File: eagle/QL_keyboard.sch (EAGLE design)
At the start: 40 parts, among them J1 USB-A-S, J2 AVR_SPI_PRG_6TESTPOINTS, U2 3.3V/150mA, U3 MAX3421ESMD, U4 ATMEGA328P_TQFP, U5 TXB0108PW-TSSOP20, Y1 8MHZ

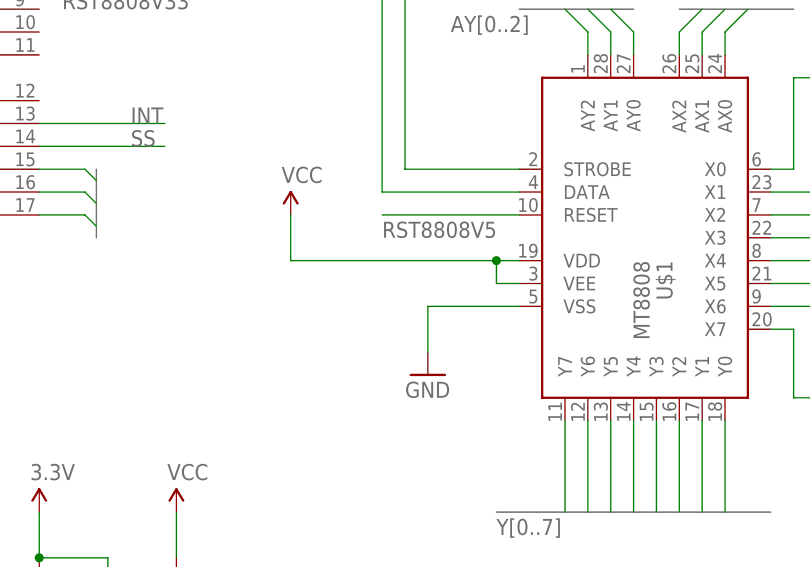
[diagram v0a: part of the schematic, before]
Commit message: Fix bug in MT8808 VEE connection: connect to GND instead of VCC
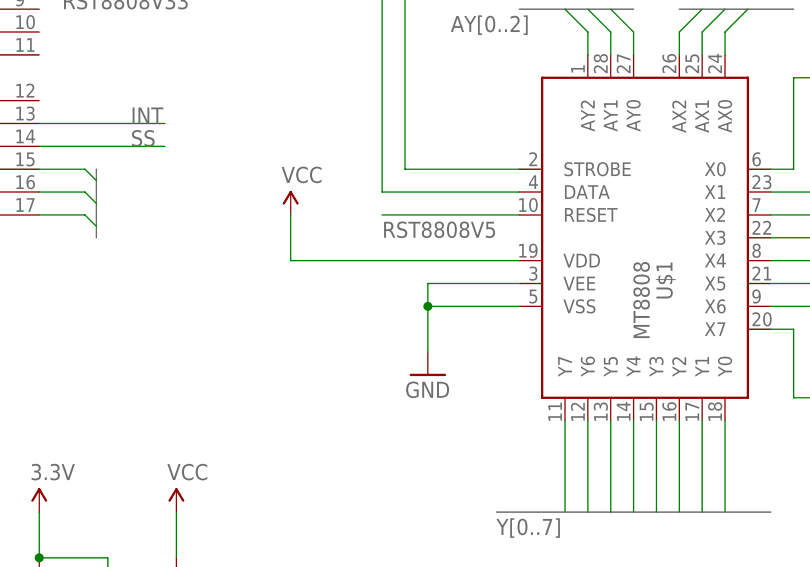
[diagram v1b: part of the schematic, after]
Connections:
- net GND: now also U$1.VEE
- net VCC: no longer U$1.VEE
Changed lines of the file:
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@@
 <pinref part="U$1" gate="G$1" pin="VDD"/>
 <pinref part="SUPPLY3" gate="G$1" pin="VCC"/>
-<wire x1="111.76" y1="35.56" x2="109.22" y2="35.56" width="0.1524" layer="91"/>
-<wire x1="109.22" y1="35.56" x2="86.36" y2="35.56" width="0.1524" layer="91"/>
+<wire x1="111.76" y1="35.56" x2="86.36" y2="35.56" width="0.1524" layer="91"/>
 <wire x1="86.36" y1="35.56" x2="86.36" y2="40.64" width="0.1524" layer="91"/>
-<pinref part="U$1" gate="G$1" pin="VEE"/>
-<wire x1="111.76" y1="33.02" x2="109.22" y2="33.02" width="0.1524" layer="91"/>
-<wire x1="109.22" y1="33.02" x2="109.22" y2="35.56" width="0.1524" layer="91"/>
-<junction x="109.22" y="35.56"/>
 </segment>
 <segment>
@@
 <wire x1="111.76" y1="30.48" x2="101.6" y2="30.48" width="0.1524" layer="91"/>
 <wire x1="101.6" y1="30.48" x2="101.6" y2="25.4" width="0.1524" layer="91"/>
+<pinref part="U$1" gate="G$1" pin="VEE"/>
+<wire x1="111.76" y1="33.02" x2="101.6" y2="33.02" width="0.1524" layer="91"/>
+<wire x1="101.6" y1="33.02" x2="101.6" y2="30.48" width="0.1524" layer="91"/>
+<junction x="101.6" y="30.48"/>
 </segment>
 <segment>

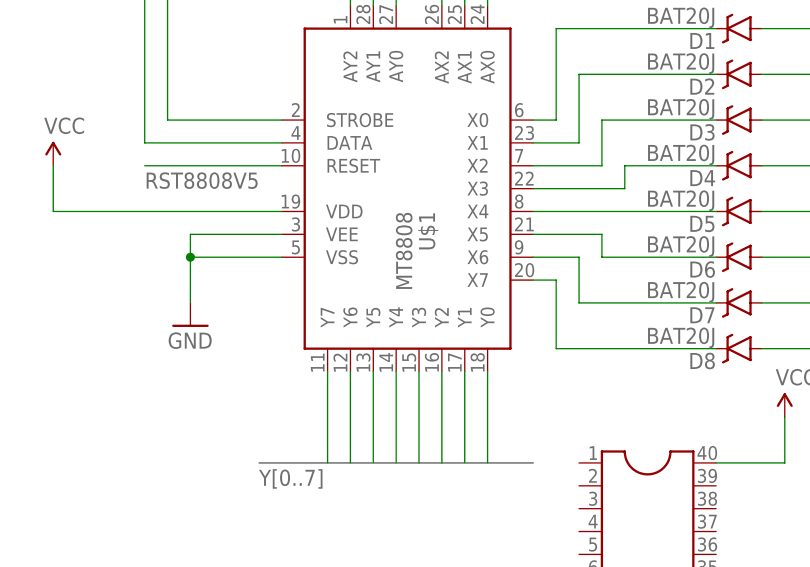
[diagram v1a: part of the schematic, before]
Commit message: Change MT8808 package to SMD PLCC28 holder.
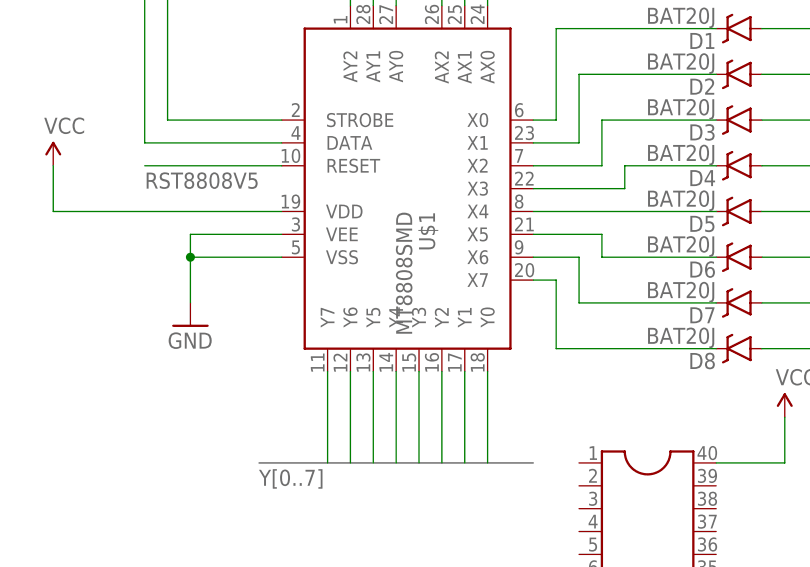
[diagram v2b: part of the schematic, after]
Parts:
- U$1: value MT8808 -> MT8808SMD; device ppe_custom:MT8808 -> ppe_custom:MT8808SMD

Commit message: Replace FTDI header with a two pin RXI/TXO header.
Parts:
- removed C10: 0.1uF, SparkFun-Capacitors:2.2UF-10V-20%(0603)
- removed FTDI: 1, SparkFun-Connectors:ARDUINO_SERIAL_PROGRAMPTH
- added COMMS: (no value), ppe_custom:M02PTH
- Y1: device SparkFun-FreqCtrl:RESONATOR8MHZ -> ppe_custom:RESONATOR8MHZ
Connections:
- removed net DTR: C10.1, FTDI.DTR
- net 3.3V: no longer FTDI.VCC
- net GND: no longer FTDI.CTS, FTDI.GND
- net RST: no longer C10.2
- net RXI: now also COMMS.1; no longer FTDI.RXI
- net TXO: now also COMMS.2; no longer FTDI.TXO

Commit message: Move ISP header and fix USB connector footprint
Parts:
- J1: device SparkFun-Connectors:USB-A-S -> ppe_custom:USB-A-S
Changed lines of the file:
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@@
 <part name="U3" library="SparkFun-DigitalIC" deviceset="MAX3421E" device="SMD"/>
 <part name="U4" library="SparkFun-DigitalIC" deviceset="ATMEGA328P_TQFP" device="" value="ATMEGA328P_TQFP"/>
-<part name="J1" library="SparkFun-Connectors" deviceset="USB" device="-A-S"/>
 <part name="R3" library="SparkFun-Resistors" deviceset="33OHM1/10W1%(0603)" device="" value="33"/>
 <part name="R4" library="SparkFun-Resistors" deviceset="33OHM1/10W1%(0603)" device="" value="33"/>
@@
 <part name="Y1" library="ppe_custom" deviceset="RESONATOR" device="8MHZ" value="8MHZ"/>
 <part name="COMMS" library="ppe_custom" deviceset="M02" device="PTH"/>
+<part name="J1" library="ppe_custom" deviceset="USB" device="-A-S"/>
 </parts>
 <sheets>
@@
 <instance part="U3" gate="G$1" x="-27.94" y="73.66" rot="R90"/>
 <instance part="U4" gate="U$1" x="35.56" y="68.58"/>
-<instance part="J1" gate="G$1" x="-68.58" y="43.18" rot="R180"/>
 <instance part="R3" gate="G$1" x="-46.99" y="38.1"/>
 <instance part="R4" gate="G$1" x="-46.99" y="30.48"/>
@@
 <instance part="Y1" gate="G$1" x="5.08" y="63.5"/>
 <instance part="COMMS" gate="G$1" x="86.36" y="-38.1"/>
+<instance part="J1" gate="G$1" x="-68.58" y="43.18" rot="R180"/>
 </instances>
 <busses>
@@
 <net name="N$1" class="0">
 <segment>
-<pinref part="J1" gate="G$1" pin="D-"/>
 <pinref part="R3" gate="G$1" pin="1"/>
 <wire x1="-66.04" y1="38.1" x2="-52.07" y2="38.1" width="0.1524" layer="91"/>
+<pinref part="J1" gate="G$1" pin="D-"/>
 </segment>
 </net>
@@
 <wire x1="-52.07" y1="30.48" x2="-55.88" y2="30.48" width="0.1524" layer="91"/>
 <wire x1="-55.88" y1="30.48" x2="-55.88" y2="35.56" width="0.1524" layer="91"/>
+<wire x1="-55.88" y1="35.56" x2="-66.04" y2="35.56" width="0.1524" layer="91"/>
 <pinref part="J1" gate="G$1" pin="D+"/>
-<wire x1="-55.88" y1="35.56" x2="-66.04" y2="35.56" width="0.1524" layer="91"/>
 </segment>
 </net>
@@
 </segment>
 <segment>
-<pinref part="J1" gate="G$1" pin="VBUS"/>
 <wire x1="-54.61" y1="40.64" x2="-66.04" y2="40.64" width="0.1524" layer="91"/>
 <label x="-59.69" y="40.64" size="1.778" layer="95"/>
+<pinref part="J1" gate="G$1" pin="VBUS"/>
 </segment>
 </net>
@@
 <wire x1="-53.34" y1="22.86" x2="-53.34" y2="43.18" width="0.1524" layer="91"/>
 <pinref part="C3" gate="G$1" pin="1"/>
-<pinref part="J1" gate="G$1" pin="GND"/>
 <wire x1="-53.34" y1="43.18" x2="-53.34" y2="46.99" width="0.1524" layer="91"/>
 <wire x1="-66.04" y1="43.18" x2="-53.34" y2="43.18" width="0.1524" layer="91"/>
 <junction x="-53.34" y="43.18"/>
-</segment>
-<segment>
+<pinref part="J1" gate="G$1" pin="GND"/>
+</segment>
+<segment>

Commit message: General cleanup of layout
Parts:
- renumbered XTAL-12MHZ to U$3
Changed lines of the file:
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@@
 <setting verticaltext="up"/>
 </settings>
-<grid distance="0.1" unitdist="inch" unit="inch" style="lines" multiple="1" display="no" altdistance="0.01" altunitdist="inch" altunit="inch"/>
+<grid distance="5" unitdist="mil" unit="mil" style="lines" multiple="1" display="no" altdistance="0.01" altunitdist="inch" altunit="inch"/>
 <layers>
 <layer number="1" name="Top" color="4" fill="1" visible="no" active="no"/>
@@
 <part name="GND3" library="SparkFun-Aesthetics" deviceset="GND" device=""/>
 <part name="SUPPLY5" library="SparkFun-Aesthetics" deviceset="3.3V" device=""/>
-<part name="XTAL-12MHZ" library="ppe_custom" deviceset="CRYSTAL-SMD" device=""/>
 <part name="GND4" library="SparkFun-Aesthetics" deviceset="GND" device=""/>
 <part name="GND5" library="SparkFun-Aesthetics" deviceset="GND" device=""/>
@@
 <part name="COMMS" library="ppe_custom" deviceset="M02" device="PTH"/>
 <part name="J1" library="ppe_custom" deviceset="USB" device="-A-S"/>
+<part name="U$3" library="ppe_custom" deviceset="CRYSTAL-SMD" device=""/>
 </parts>
 <sheets>
@@
 <instance part="GND3" gate="1" x="-71.12" y="102.87"/>
 <instance part="SUPPLY5" gate="G$1" x="-33.02" y="123.19"/>
-<instance part="XTAL-12MHZ" gate="G$1" x="-44.45" y="-11.43"/>
 <instance part="GND4" gate="1" x="-44.45" y="-26.67"/>
 <instance part="GND5" gate="1" x="-7.62" y="38.1"/>
@@
 <instance part="COMMS" gate="G$1" x="86.36" y="-38.1"/>
 <instance part="J1" gate="G$1" x="-68.58" y="43.18" rot="R180"/>
+<instance part="U$3" gate="G$1" x="-44.45" y="-11.43"/>
 </instances>
 <busses>
@@
 </segment>
 <segment>
-<pinref part="XTAL-12MHZ" gate="G$1" pin="1"/>
 <pinref part="C1" gate="G$1" pin="1"/>
 <wire x1="-46.99" y1="-11.43" x2="-54.61" y2="-11.43" width="0.1524" layer="91"/>
@@
 <junction x="-54.61" y="-11.43"/>
 <label x="-55.88" y="-6.35" size="1.778" layer="95" rot="R90"/>
+<pinref part="U$3" gate="G$1" pin="1"/>
 </segment>
 </net>
@@
 </segment>
 <segment>
-<pinref part="XTAL-12MHZ" gate="G$1" pin="2"/>
 <pinref part="C2" gate="G$1" pin="1"/>
 <wire x1="-41.91" y1="-11.43" x2="-34.29" y2="-11.43" width="0.1524" layer="91"/>
@@
 <junction x="-34.29" y="-11.43"/>
 <label x="-35.56" y="-6.35" size="1.778" layer="95" rot="R90"/>
-</segment>
-</net>
+<pinref part="U$3" gate="G$1" pin="2"/>
+</segment>
+</net>

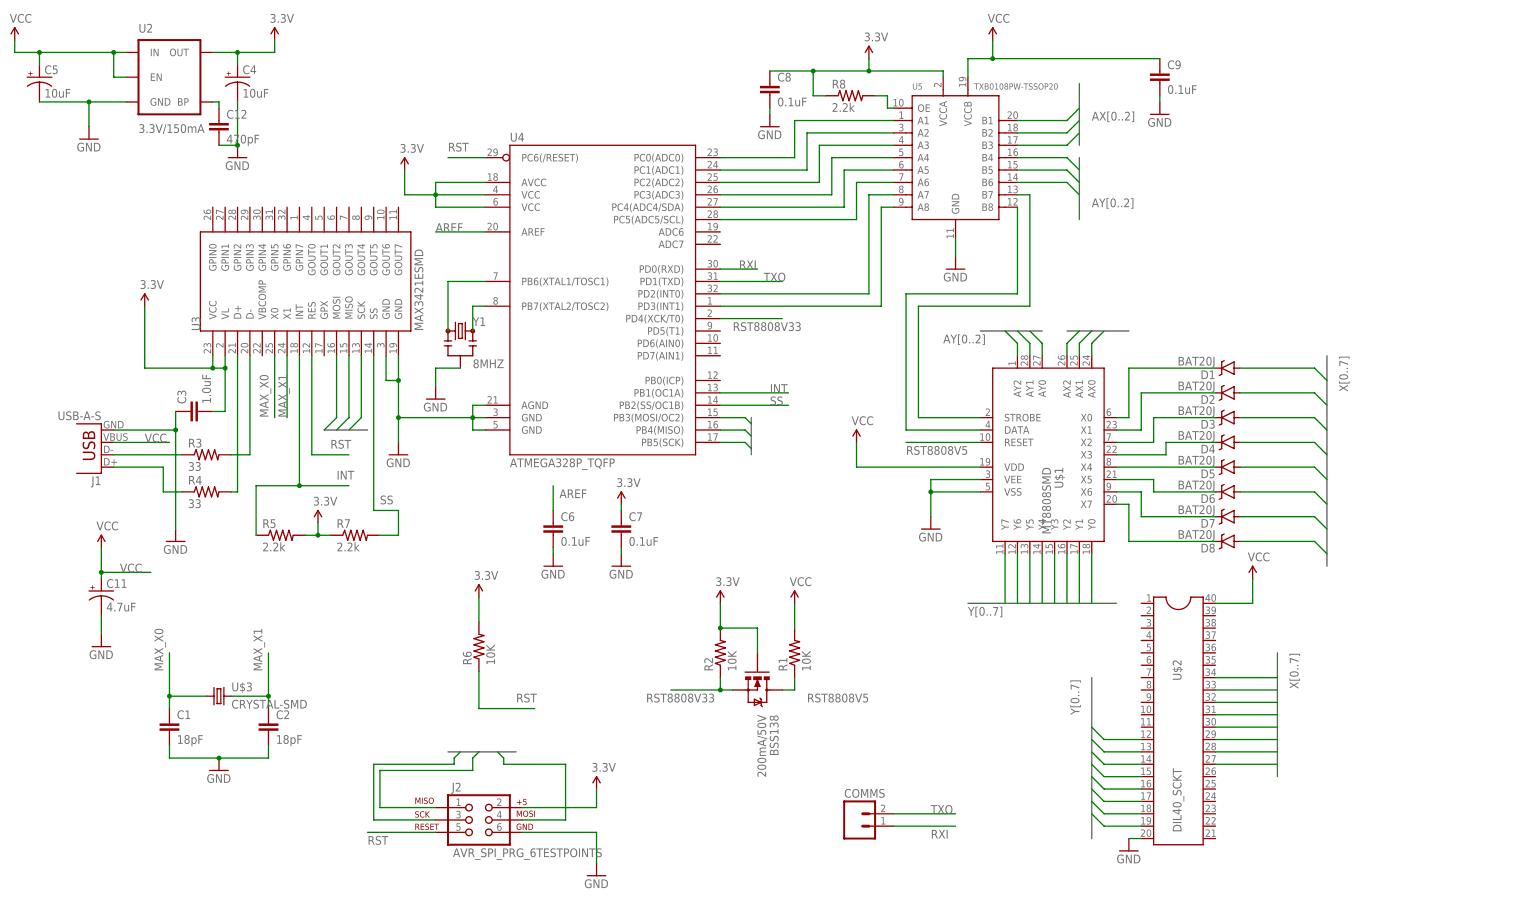
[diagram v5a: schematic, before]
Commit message: Add QL reset logic with voltage level shifting.
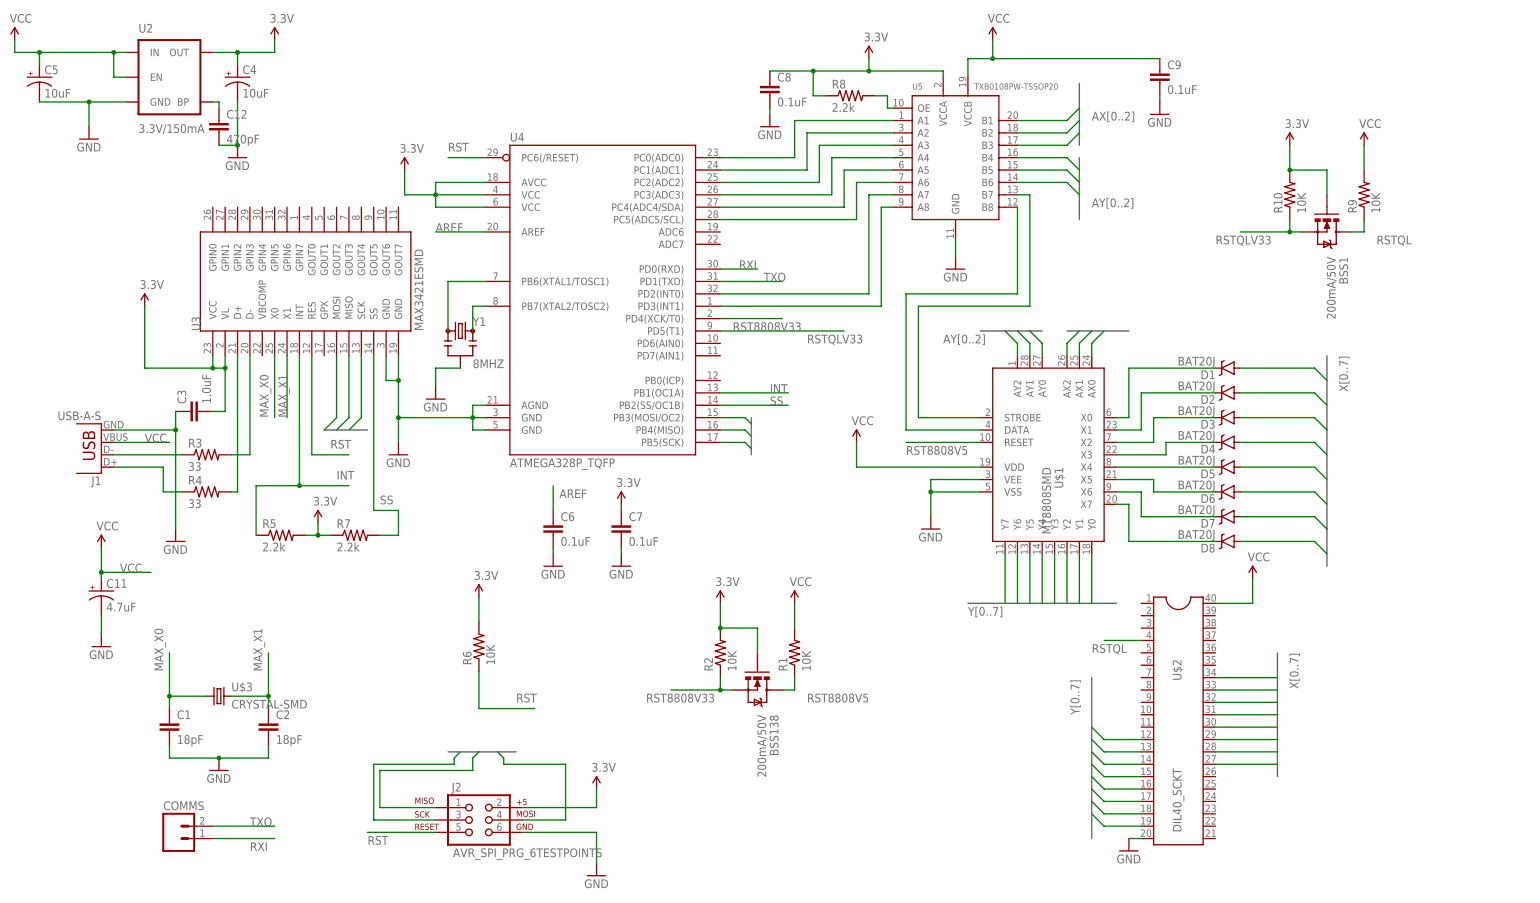
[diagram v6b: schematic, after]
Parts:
- added BSS1: 200mA/50V, SparkFun-DiscreteSemi:MOSFET-NCHANNELBSS138
- added R10, R9: 10K, SparkFun-Resistors:10KOHM-1/10W-1%(0603)0603
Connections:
- new net RSTQL: BSS1.D, R9.1, U$2.4
- new net RSTQLV33: BSS1.S, R10.1, U4.PD5(T1)
- net 3.3V: now also BSS1.G, R10.2
- net VCC: now also R9.2
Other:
- moved on the sheet: COMMS
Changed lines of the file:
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@@
 <setting verticaltext="up"/>
 </settings>
-<grid distance="5" unitdist="mil" unit="mil" style="lines" multiple="1" display="no" altdistance="0.01" altunitdist="inch" altunit="inch"/>
+<grid distance="0.1" unitdist="inch" unit="inch" style="lines" multiple="1" display="no" altdistance="0.01" altunitdist="inch" altunit="inch"/>
 <layers>
 <layer number="1" name="Top" color="4" fill="1" visible="no" active="no"/>
@@
 <part name="J1" library="ppe_custom" deviceset="USB" device="-A-S"/>
 <part name="U$3" library="ppe_custom" deviceset="CRYSTAL-SMD" device=""/>
+<part name="BSS1" library="SparkFun-DiscreteSemi" deviceset="MOSFET-NCHANNEL" device="BSS138" value="200mA/50V"/>
+<part name="R9" library="SparkFun-Resistors" deviceset="10KOHM-1/10W-1%(0603)" device="0603" value="10K"/>
+<part name="R10" library="SparkFun-Resistors" deviceset="10KOHM-1/10W-1%(0603)" device="0603" value="10K"/>
+<part name="SUPPLY16" library="SparkFun-Aesthetics" deviceset="VCC" device=""/>
+<part name="SUPPLY17" library="SparkFun-Aesthetics" deviceset="3.3V" device=""/>
 </parts>
 <sheets>
@@
 <instance part="U$1" gate="G$1" x="127" y="38.1" rot="R270"/>
 <instance part="Y1" gate="G$1" x="5.08" y="63.5"/>
-<instance part="COMMS" gate="G$1" x="86.36" y="-38.1"/>
+<instance part="COMMS" gate="G$1" x="-53.34" y="-40.64"/>
 <instance part="J1" gate="G$1" x="-68.58" y="43.18" rot="R180"/>
 <instance part="U$3" gate="G$1" x="-44.45" y="-11.43"/>
+<instance part="BSS1" gate="G$1" x="182.88" y="83.82" rot="R270"/>
+<instance part="R9" gate="G$1" x="190.5" y="91.44" rot="R90"/>
+<instance part="R10" gate="G$1" x="175.26" y="91.44" rot="R90"/>
+<instance part="SUPPLY16" gate="G$1" x="190.5" y="101.6"/>
+<instance part="SUPPLY17" gate="G$1" x="175.26" y="101.6"/>
 </instances>
 <busses>
@@
 <label x="-59.69" y="40.64" size="1.778" layer="95"/>
 <pinref part="J1" gate="G$1" pin="VBUS"/>
+</segment>
+<segment>
+<pinref part="R9" gate="G$1" pin="2"/>
+<pinref part="SUPPLY16" gate="G$1" pin="VCC"/>
+<wire x1="190.5" y1="96.52" x2="190.5" y2="101.6" width="0.1524" layer="91"/>
 </segment>
 </net>
@@
 <wire x1="-6.35" y1="91.44" x2="-6.35" y2="96.52" width="0.1524" layer="91"/>
 </segment>
+<segment>
+<pinref part="R10" gate="G$1" pin="2"/>
+<pinref part="BSS1" gate="G$1" pin="G"/>
+<wire x1="175.26" y1="96.52" x2="182.88" y2="96.52" width="0.1524" layer="91"/>
+<wire x1="182.88" y1="96.52" x2="182.88" y2="91.44" width="0.1524" layer="91"/>
+<pinref part="SUPPLY17" gate="G$1" pin="3.3V"/>
+<wire x1="175.26" y1="101.6" x2="175.26" y2="96.52" width="0.1524" layer="91"/>
+<junction x="175.26" y="96.52"/>
+</segment>
 </net>
 <net name="SS" class="0">
@@
 <segment>
 <pinref part="COMMS" gate="G$1" pin="2"/>
-<wire x1="93.98" y1="-35.56" x2="106.68" y2="-35.56" width="0.1524" layer="91"/>
-<label x="101.6" y="-35.56" size="1.778" layer="95"/>
+<wire x1="-45.72" y1="-38.1" x2="-33.02" y2="-38.1" width="0.1524" layer="91"/>
+<label x="-38.1" y="-38.1" size="1.778" layer="95"/>
 </segment>
 </net>
@@
 <segment>
 <pinref part="COMMS" gate="G$1" pin="1"/>
-<wire x1="93.98" y1="-38.1" x2="106.68" y2="-38.1" width="0.1524" layer="91"/>
-<label x="101.6" y="-40.64" size="1.778" layer="95"/>
+<wire x1="-45.72" y1="-40.64" x2="-33.02" y2="-40.64" width="0.1524" layer="91"/>
+<label x="-38.1" y="-43.18" size="1.778" layer="95"/>
 </segment>
 </net>
@@
 </segment>
 </net>
+<net name="RSTQLV33" class="0">
+<segment>
+<pinref part="U4" gate="U$1" pin="PD5(T1)"/>
+<wire x1="58.42" y1="63.5" x2="83.82" y2="63.5" width="0.1524" layer="91"/>
+<label x="76.2" y="60.96" size="1.778" layer="95"/>
+</segment>
+<segment>
+<pinref part="R10" gate="G$1" pin="1"/>
+<pinref part="BSS1" gate="G$1" pin="S"/>
+<wire x1="175.26" y1="86.36" x2="175.26" y2="83.82" width="0.1524" layer="91"/>
+<wire x1="175.26" y1="83.82" x2="177.8" y2="83.82" width="0.1524" layer="91"/>
+<wire x1="175.26" y1="83.82" x2="165.1" y2="83.82" width="0.1524" layer="91"/>
+<junction x="175.26" y="83.82"/>
+<label x="160.02" y="81.28" size="1.778" layer="95"/>
+</segment>
+</net>
+<net name="RSTQL" class="0">
+<segment>
+<pinref part="U$2" gate="G$1" pin="4"/>
+<wire x1="144.78" y1="0" x2="137.16" y2="0" width="0.1524" layer="91"/>
+<label x="134.62" y="-2.54" size="1.778" layer="95"/>
+</segment>
+<segment>
+<pinref part="R9" gate="G$1" pin="1"/>
+<pinref part="BSS1" gate="G$1" pin="D"/>
+<wire x1="190.5" y1="86.36" x2="190.5" y2="83.82" width="0.1524" layer="91"/>
+<wire x1="190.5" y1="83.82" x2="187.96" y2="83.82" width="0.1524" layer="91"/>
+<label x="193.04" y="81.28" size="1.778" layer="95"/>
+</segment>
+</net>
